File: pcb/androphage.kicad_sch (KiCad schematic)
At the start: 0 parts

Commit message: - Adapt nrfmicro schematic for control and power components. - Copy key matrix schematics from old KiCAD project.
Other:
- added sheet Control (control.kicad_sch)
- added sheet Left_Switches (left_switches.kicad_sch)
- added sheet Right_Switches (right_switches.kicad_sch)
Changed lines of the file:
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@@
 	(generator_version "9.0")
 	(paper "A4")
+	(sheet
+		(at 105.41 16.51)
+		(size 39.37 22.86)
+		(exclude_from_sim no)
+		(in_bom yes)
+		(on_board yes)
+		(dnp no)
+		(fields_autoplaced yes)
+		(stroke
+			(width 0.1524)
+			(type solid)
+		)
+		(fill
+			(color 0 0 0 0.0000)
+		)
+		(property "Sheetname" "Right_Switches"
+			(at 105.41 15.7984 0)
+			(effects
+				(font
+					(size 1.27 1.27)
+				)
+				(justify left bottom)
+			)
+		)
+		(property "Sheetfile" "right_switches.kicad_sch"
+			(at 105.41 39.9546 0)
+			(effects
+				(font
+					(size 1.27 1.27)
+				)
+				(justify left top)
+			)
+		)
+		(property "Field2" ""
+			(at 105.41 16.51 0)
+			(effects
+				(font
+					(size 1.27 1.27)
+				)
+			)
+		)
+		(instances
+			(project "androphage"
+				(path "/99196bd8-ec0c-4029-b5c4-fcab8025953e"
+					(page "4")
+				)
+			)
+		)
+	)
+	(sheet
+		(at 16.51 16.51)
+		(size 40.64 22.86)
+		(exclude_from_sim no)
+		(in_bom yes)
+		(on_board yes)
+		(dnp no)
+		(fields_autoplaced yes)
+		(stroke
+			(width 0.1524)
+			(type solid)
+		)
+		(fill
+			(color 0 0 0 0.0000)
+		)
+		(property "Sheetname" "Control"
+			(at 16.51 15.7984 0)
+			(effects
+				(font
+					(size 1.27 1.27)
+				)
+				(justify left bottom)
+			)
+		)
+		(property "Sheetfile" "control.kicad_sch"
+			(at 16.51 39.9546 0)
+			(effects
+				(font
+					(size 1.27 1.27)
+				)
+				(justify left top)
+			)
+		)
+		(instances
+			(project "androphage"
+				(path "/99196bd8-ec0c-4029-b5c4-fcab8025953e"
+					(page "2")
+				)
+			)
+		)
+	)
+	(sheet
+		(at 62.23 16.51)
+		(size 39.37 22.86)
+		(exclude_from_sim no)
+		(in_bom yes)
+		(on_board yes)
+		(dnp no)
+		(fields_autoplaced yes)
+		(stroke
+			(width 0.1524)
+			(type solid)
+		)
+		(fill
+			(color 0 0 0 0.0000)
+		)
+		(property "Sheetname" "Left_Switches"
+			(at 62.23 15.7984 0)
+			(effects
+				(font
+					(size 1.27 1.27)
+				)
+				(justify left bottom)
+			)
+		)
+		(property "Sheetfile" "left_switches.kicad_sch"
+			(at 62.23 39.9546 0)
+			(effects
+				(font
+					(size 1.27 1.27)
+				)
+				(justify left top)
+			)
+		)
+		(instances
+			(project "androphage"
+				(path "/99196bd8-ec0c-4029-b5c4-fcab8025953e"
+					(page "3")
+				)
+			)
+		)
+	)
 	(sheet_instances
 		(path "/"

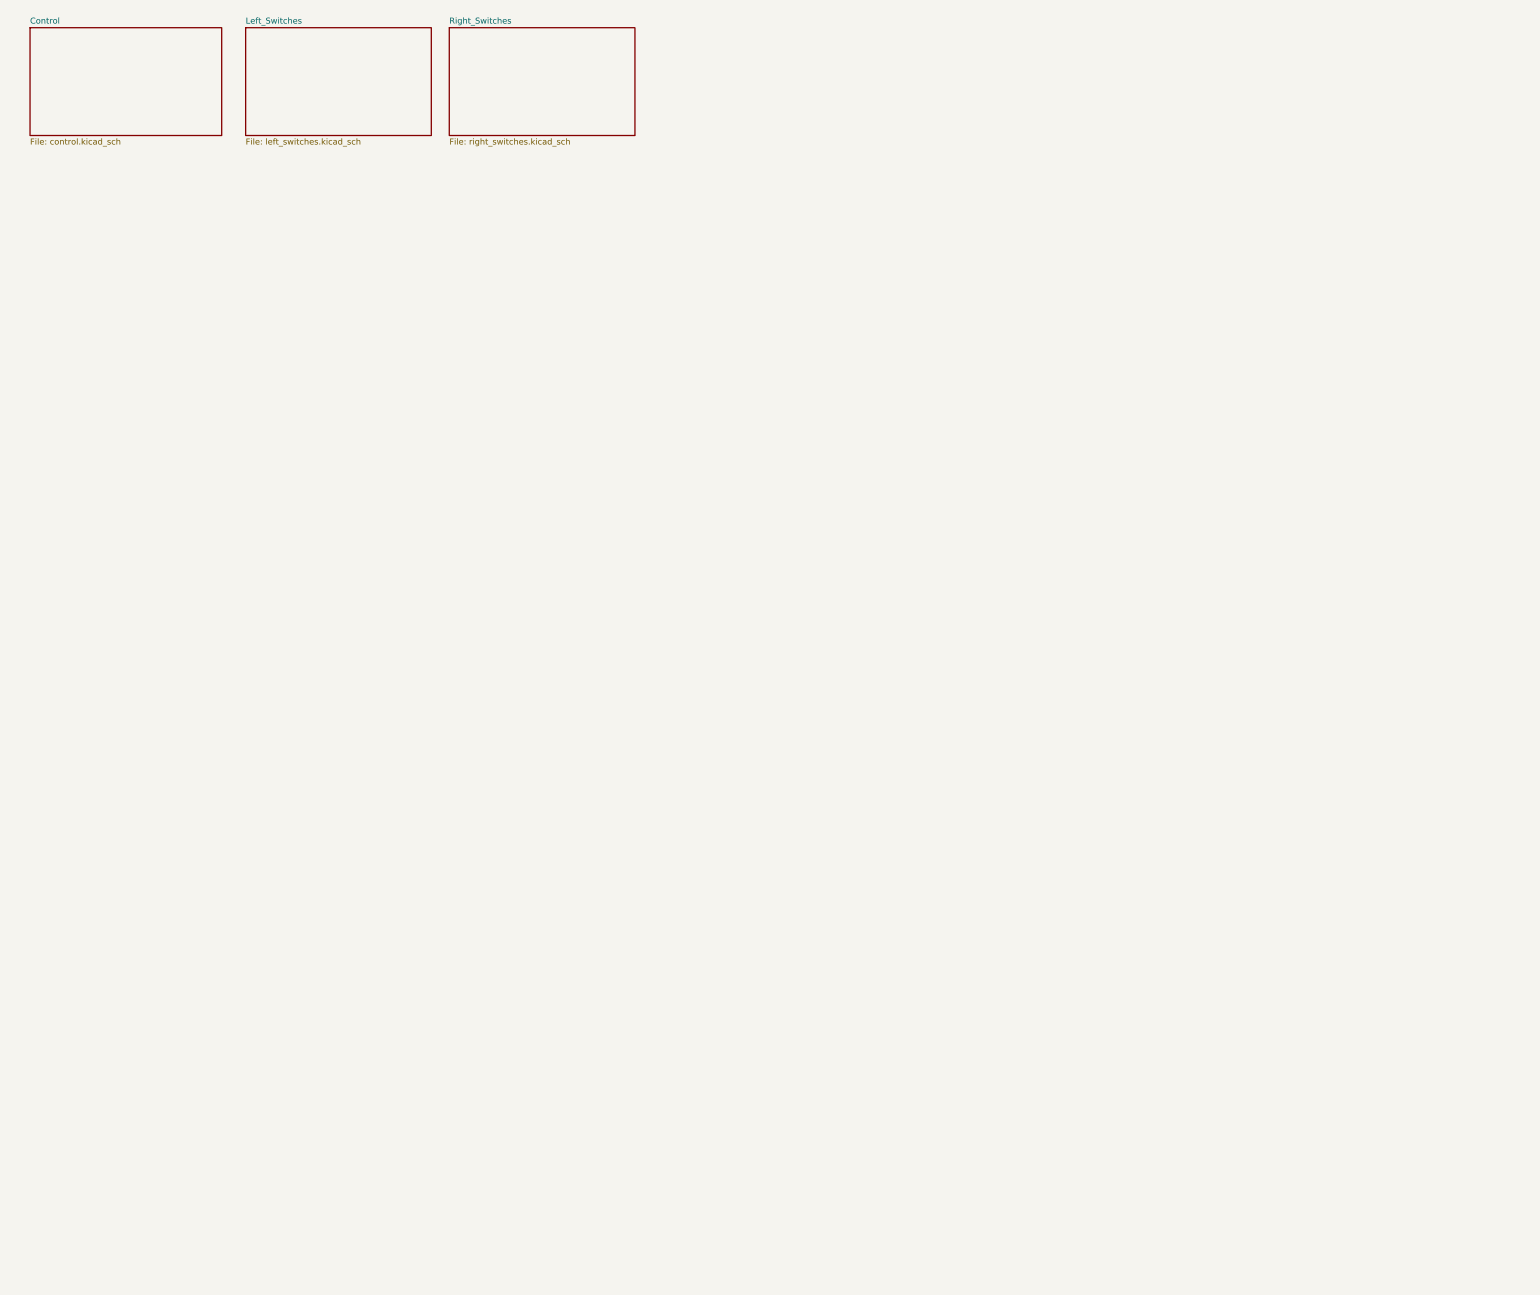
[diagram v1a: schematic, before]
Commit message: Complete preliminary PCB schematic.
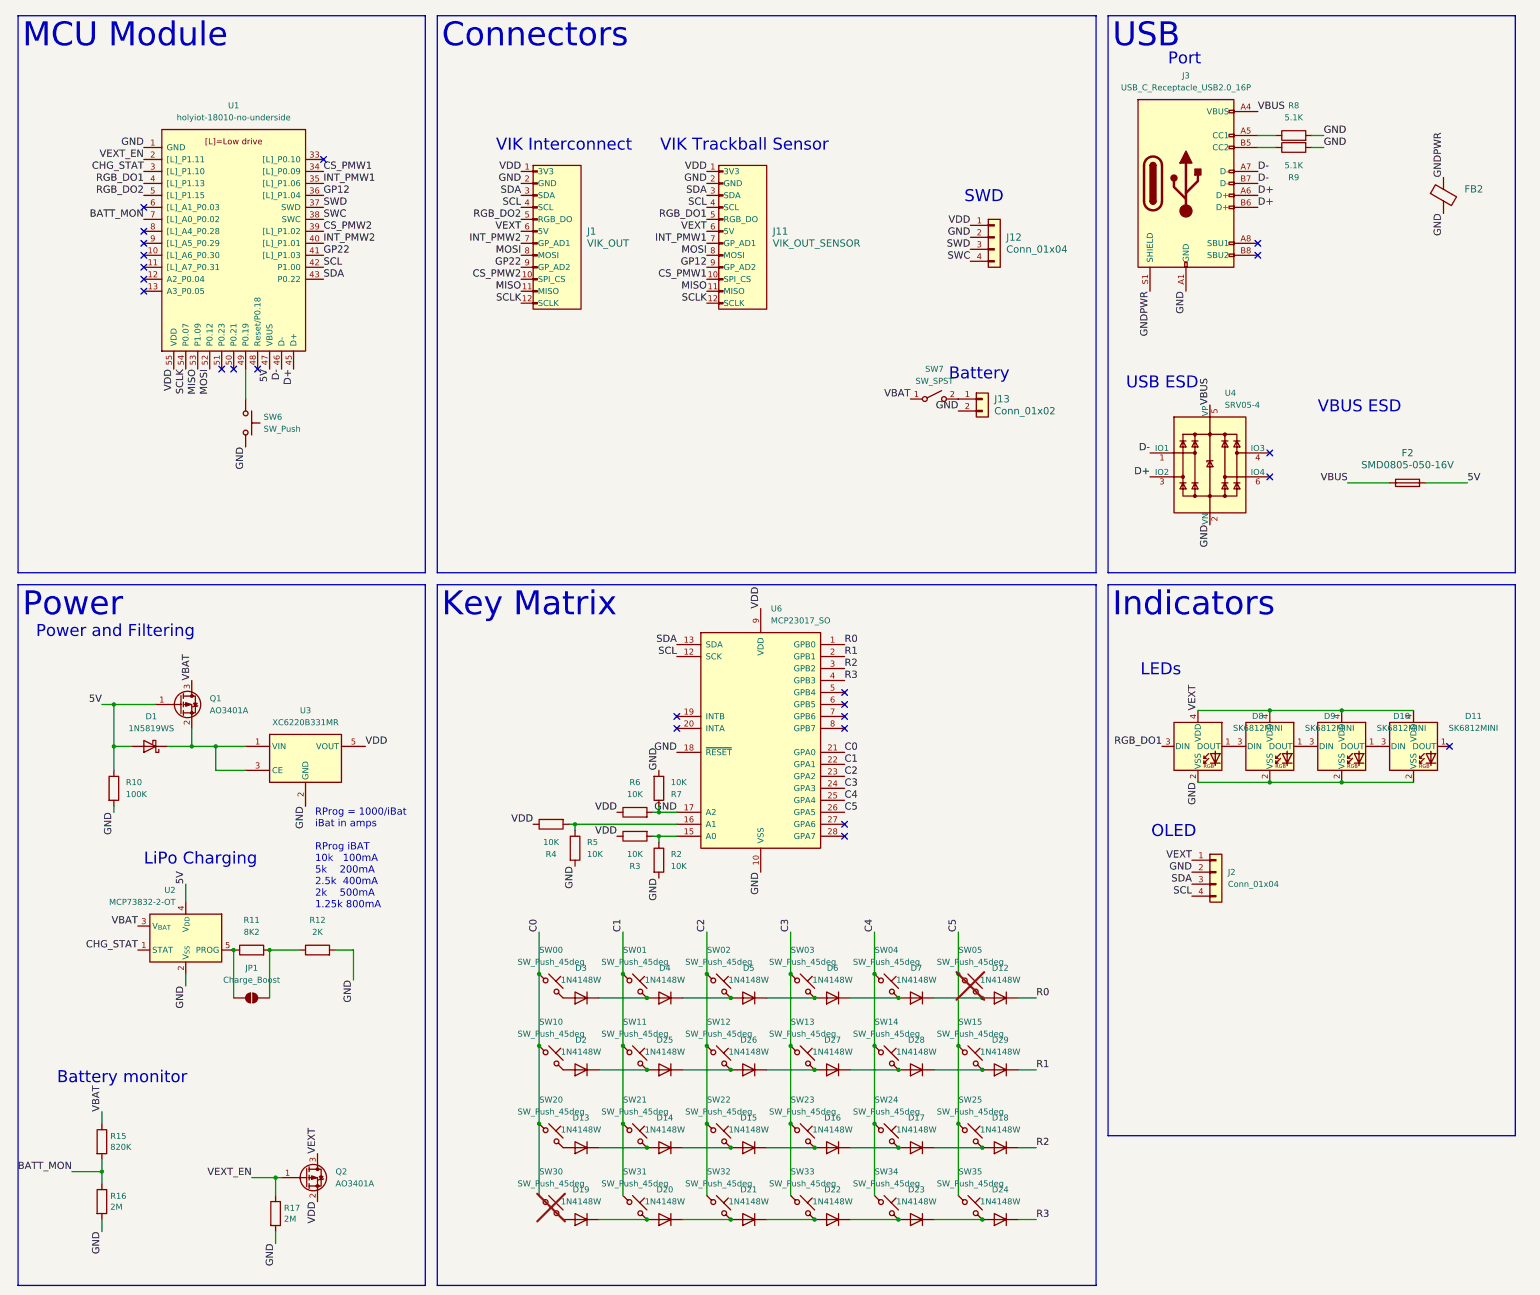
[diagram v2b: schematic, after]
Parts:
- added D1: 1N5819WS, Diode_SMD:D_SOD-323, symbol Diode:1N5819WS
- added D10, D11, D8, D9: SK6812MINI, LED_SMD:LED_SK6812MINI_PLCC4_3.5x3.5mm_P1.75mm, symbol LED:SK6812MINI
- added D12, D13, D14, D15, D16, D17, D18, D19, D2, D20, D21, D22, D23, D24, D25, D26, D27, D28, D29, D3, D4, D5, D6, D7: 1N4148W, Diode_SMD:D_SOD-123, symbol Diode:1N4148W
- added F2: SMD0805-050-16V, Fuse:Fuse_0805_2012Metric, symbol Device:Fuse
- added FB2: ~, Inductor_SMD:L_0805_2012Metric, symbol Device:FerriteBead
- added J1: VIK_OUT, vik:vik-keyboard-connector-horizontal, symbol vik:vik-keyboard-connector
- added J11: VIK_OUT_SENSOR, vik:vik-keyboard-connector-horizontal, symbol vik:vik-keyboard-connector
- added J12: Conn_01x04, Connector_PinSocket_2.54mm:PinSocket_1x04_P2.54mm_Vertical, symbol Connector_Generic:Conn_01x04
- added J13: Conn_01x02, Connector_JST:JST_GH_SM02B-GHS-TB_1x02-1MP_P1.25mm_Horizontal, symbol Connector_Generic:Conn_01x02
- added J2: Conn_01x04, Connector_JST:JST_GH_SM04B-GHS-TB_1x04-1MP_P1.25mm_Horizontal, symbol Connector_Generic:Conn_01x04
- added J3: USB_C_Receptacle_USB2.0_16P, Connector_USB:USB_C_Receptacle_HRO_TYPE-C-31-M-12, symbol Connector:USB_C_Receptacle_USB2.0_16P
- added JP1: Charge_Boost, Jumper:SolderJumper-2_P1.3mm_Open_RoundedPad1.0x1.5mm, symbol Jumper:SolderJumper_2_Open
- added Q1, Q2: AO3401A, Package_TO_SOT_SMD:SOT-23, symbol Transistor_FET:AO3401A
- added R10: 100K, Resistor_SMD:R_0201_0603Metric_Pad0.64x0.40mm_HandSolder, symbol Device:R
- added R11: 8K2, Resistor_SMD:R_0201_0603Metric_Pad0.64x0.40mm_HandSolder, symbol Device:R
- added R12: 2K, Resistor_SMD:R_0201_0603Metric_Pad0.64x0.40mm_HandSolder, symbol Device:R
- added R15: 820K, Resistor_SMD:R_0603_1608Metric, symbol Device:R
- added R16, R17: 2M, Resistor_SMD:R_0603_1608Metric, symbol Device:R
- added R2, R3, R4, R5, R6, R7: 10K, Resistor_SMD:R_0201_0603Metric_Pad0.64x0.40mm_HandSolder, symbol Device:R
- added R8, R9: 5.1K, Resistor_SMD:R_0201_0603Metric_Pad0.64x0.40mm_HandSolder, symbol Device:R
- added SW00, SW01, SW02, SW03, SW04, SW10, SW11, SW12, SW13, SW14, SW15, SW20, SW21, SW22, SW23, SW24, SW25, SW31, SW32, SW33, SW34, SW35: SW_Push_45deg, key-switches:SW_GLP_Kailh_Choc_V1V2_HotSwap_double, symbol Switch:SW_Push_45deg
- added SW05, SW30: SW_Push_45deg, symbol Switch:SW_Push_45deg
- added SW6: SW_Push, Button_Switch_SMD:SW_Push_1P1T_NO_E-Switch_TL3301NxxxxxG, symbol Switch:SW_Push
- added SW7: SW_SPST, library:AS11CH, symbol Switch:SW_SPST
- added U1: holyiot-18010-no-underside, mcu:holyiot-18010-no-underside, symbol mcu:holyiot-18010-no-underside
- added U2: MCP73832-2-OT, Package_TO_SOT_SMD:SOT-23-5, symbol Battery_Management:MCP73832-2-OT
- added U3: XC6220B331MR, Package_TO_SOT_SMD:SOT-23-5, symbol Regulator_Linear:XC6220B331MR
- added U4: SRV05-4, Package_TO_SOT_SMD:SOT-23-6, symbol Power_Protection:SRV05-4
- added U6: MCP23017_SO, Package_SO:SOIC-28W_7.5x17.9mm_P1.27mm, symbol Interface_Expansion:MCP23017_SO
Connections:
- new net: D23.1 (K), D24.2 (A), SW35.2
- new net: R4.2, R5.1, U6.16 (A1)
- new net: D6.1 (K), D7.2 (A), SW04.2
- new net: D5.1 (K), D6.2 (A), SW03.2
- new net: R2.1, R3.2, U6.15 (A0)
- new net: SW6.1, U1.49 (P0.19)
- new net: J3.A5 (CC1), R8.1
- new net: D10.1 (DOUT), D11.3 (DIN)
- new net: D10.3 (DIN), D9.1 (DOUT)
- new net: D13.2 (A), SW20.2
- new net: D16.1 (K), D17.2 (A), SW24.2
- new net: D15.1 (K), D16.2 (A), SW23.2
- new net: J3.B5 (CC2), R9.1
- new net: D27.1 (K), D28.2 (A), SW14.2
- new net: D17.1 (K), D18.2 (A), SW25.2
- new net: D22.1 (K), D23.2 (A), SW34.2
- new net: D12.2 (A), D7.1 (K), SW05.2
- new net: D4.1 (K), D5.2 (A), SW02.2
- new net: D3.1 (K), D4.2 (A), SW01.2
- new net: D28.1 (K), D29.2 (A), SW15.2
- new net: D2.1 (K), D25.2 (A), SW11.2
- new net: D2.2 (A), SW10.2
- new net: D21.1 (K), D22.2 (A), SW33.2
- new net: D19.1 (K), D20.2 (A), SW31.2
- new net: JP1.1 (A), R11.1, U2.5 (PROG)
- new net: JP1.2 (B), R11.2, R12.1
- new net: J13.1 (Pin_1), SW7.2 (B)
- new net: D25.1 (K), D26.2 (A), SW12.2
- new net: D3.2 (A), SW00.2
- new net: D13.1 (K), D14.2 (A), SW21.2
- new net: D26.1 (K), D27.2 (A), SW13.2
- new net: D19.2 (A), SW30.2
- new net: D8.1 (DOUT), D9.3 (DIN)
- new net: D14.1 (K), D15.2 (A), SW22.2
- new net: D20.1 (K), D21.2 (A), SW32.2
- new net: D1.1 (K), Q1.2 (S), U3.1 (VIN), U3.3 (CE)
- new net 5V: D1.2 (A), F2.2, Q1.1 (G), R10.1, U1.47 (VBUS), U2.4 (V_{DD})
- new net BATT_MON: R15.2, R16.1, U1.7 ([L]_A0_P0.02)
- new net C0: SW00.1, SW10.1, SW20.1, SW30.1, U6.21 (GPA0)
- new net C1: SW01.1, SW11.1, SW21.1, SW31.1, U6.22 (GPA1)
- new net C2: SW02.1, SW12.1, SW22.1, SW32.1, U6.23 (GPA2)
- new net C3: SW03.1, SW13.1, SW23.1, SW33.1, U6.24 (GPA3)
- new net C4: SW04.1, SW14.1, SW24.1, SW34.1, U6.25 (GPA4)
- new net C5: SW05.1, SW15.1, SW25.1, SW35.1, U6.26 (GPA5)
- new net CHG_STAT: U1.3 ([L]_P1.10), U2.1 (STAT)
- new net CS_PMW1: J11.10 (SPI_CS), U1.34 ([L]_P0.09)
- new net CS_PMW2: J1.10 (SPI_CS), U1.39 ([L]_P1.02)
- new net D+: J3.A6 (D+), J3.B6 (D+), U1.45 (D+), U4.3 (IO2)
- new net D-: J3.A7 (D-), J3.B7 (D-), U1.46 (D-), U4.1 (IO1)
- new net GND: D10.2 (VSS), D11.2 (VSS), D8.2 (VSS), D9.2 (VSS), FB2.2, J1.2 (GND), J11.2 (GND), J12.2 (Pin_2), J13.2 (Pin_2), J2.2 (Pin_2), J3.A1 (GND), J3.A12 (GND), J3.B1 (GND), J3.B12 (GND), R10.2, R12.2, R16.2, R17.2, R2.2, R5.2, R6.2, R7.1, R7.2, R8.2, R9.2, SW6.2, U1.1 (GND), U1.32 (GND), U1.44 (GND), U2.2 (V_{SS}), U3.2 (GND), U4.2 (VN), U6.10 (VSS), U6.17 (A2), U6.18 (~{RESET})
- new net GNDPWR: FB2.1, J3.S1 (SHIELD)
- new net GP12: J11.9 (GP_AD2), U1.36 ([L]_P1.04)
- new net GP22: J1.9 (GP_AD2), U1.41 ([L]_P1.03)
- new net INT_PMW1: J11.7 (GP_AD1), U1.35 ([L]_P1.06)
- new net INT_PMW2: J1.7 (GP_AD1), U1.40 ([L]_P1.01)
- new net MISO: J1.11 (MISO), J11.11 (MISO), U1.53 (P1.09)
- new net MOSI: J1.8 (MOSI), J11.8 (MOSI), U1.52 (P0.12)
- new net R0: D12.1 (K), U6.1 (GPB0)
- new net R1: D29.1 (K), U6.2 (GPB1)
- new net R2: D18.1 (K), U6.3 (GPB2)
- new net R3: D24.1 (K), U6.4 (GPB3)
- new net RGB_DO1: D8.3 (DIN), J11.5 (RGB_DO), U1.4 ([L]_P1.13)
- new net RGB_DO2: J1.5 (RGB_DO), U1.5 ([L]_P1.15)
- new net SCL: J1.4 (SCL), J11.4 (SCL), J2.4 (Pin_4), U1.42 (P1.00), U6.12 (SCK)
- new net SCLK: J1.12 (SCLK), J11.12 (SCLK), U1.54 (P0.07)
- new net SDA: J1.3 (SDA), J11.3 (SDA), J2.3 (Pin_3), U1.43 (P0.22), U6.13 (SDA)
- new net SWC: J12.4 (Pin_4), U1.38 (SWC)
- new net SWD: J12.3 (Pin_3), U1.37 (SWD)
- new net VBAT: Q1.3 (D), R15.1, SW7.1 (A), U2.3 (V_{BAT})
- new net VBUS: F2.1, J3.A4 (VBUS), J3.A9 (VBUS), J3.B4 (VBUS), J3.B9 (VBUS), U4.5 (VP)
- new net VDD: J1.1 (3V3), J11.1 (3V3), J12.1 (Pin_1), Q2.2 (S), R3.1, R4.1, R6.1, U1.55 (VDD), U3.5 (VOUT), U6.9 (VDD)
- new net VEXT: D10.4 (VDD), D11.4 (VDD), D8.4 (VDD), D9.4 (VDD), J1.6 (5V), J11.6 (5V), J2.1 (Pin_1), Q2.3 (D)
- new net VEXT_EN: Q2.1 (G), R17.1, U1.2 ([L]_P1.11)
- no-connect marks 0 -> 24
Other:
- removed sheet Control
- removed sheet Left_Switches
- removed sheet Right_Switches
- note added: "Battery"
- note added: "Battery monitor"
- note added: "LEDs"
- note added: "LiPo Charging"
- note added: "OLED"
- note added: "Port"
- note added: "Power and Filtering"
- note added: "RProg = 1000/iBat iBat in amps RProg iBAT 10k 100mA 5k 200mA 2.5k 400mA 2k 500mA 1.25k 800mA"
- note added: "SWD"
- note added: "USB ESD"
- note added: "VBUS ESD"
- note added: "VIK Interconnect"
- note added: "VIK Trackball Sensor"

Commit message: Start PCB layout.
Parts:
- added R1: 10K, Resistor_SMD:R_0201_0603Metric_Pad0.64x0.40mm_HandSolder, symbol Device:R
- U6: value MCP23017_SO -> MCP23017_SS; footprint Package_SO:SOIC-28W_7.5x17.9mm_P1.27mm -> Package_SO:SSOP-28_5.3x10.2mm_P0.65mm; symbol Interface_Expansion:MCP23017_SO -> Interface_Expansion:MCP23017_SS
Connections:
- net GND: no longer U6.18 (~{RESET})
- net VDD: now also R1.1
- new net: R1.2, U6.18 (~{RESET})
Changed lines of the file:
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@@
 	(wire
 		(pts
+			(xy 151.13 167.64) (xy 151.13 170.18)
+		)
+		(stroke
+			(width 0)
+			(type default)
+		)
+	)
+	(wire
+		(pts
 			(xy 172.72 254) (xy 182.88 254)
 		)
@@
 	(wire
 		(pts
+			(xy 151.13 170.18) (xy 153.67 170.18)
+		)
+		(stroke
+			(width 0)
+			(type default)
+		)
+	)
+	(wire
+		(pts
 			(xy 132.08 186.69) (xy 132.08 185.42)
 		)
@@
 		)
 	)
-	(label "GND"
-		(at 153.67 170.18 180)
-		(effects
-			(font
-				(size 1.524 1.524)
-			)
-			(justify right bottom)
-		)
-	)
 	(label "VDD"
 		(at 140.97 182.88 180)
@@
 		)
 	)
+	(label "VDD"
+		(at 143.51 167.64 180)
+		(effects
+			(font
+				(size 1.524 1.524)
+			)
+			(justify right bottom)
+		)
+	)
 	(symbol
 		(lib_id "Switch:SW_Push_45deg")
@@
 	)
 	(symbol
-		(lib_id "Interface_Expansion:MCP23017_SO")
+		(lib_id "Interface_Expansion:MCP23017_SS")
 		(at 171.45 167.64 0)
 		(unit 1)
@@
 			)
 		)
-		(property "Value" "MCP23017_SO"
+		(property "Value" "MCP23017_SS"
 			(at 173.5933 142.24 0)
 			(effects
@@
 			)
 		)
-		(property "Footprint" "Package_SO:SOIC-28W_7.5x17.9mm_P1.27mm"
+		(property "Footprint" "Package_SO:SSOP-28_5.3x10.2mm_P0.65mm"
 			(at 176.53 193.04 0)
 			(effects
@@
 			)
 		)
-		(property "Description" "16-bit I/O expander, I2C, interrupts, w pull-ups, GPA/B7 output only (https://microchip.my.site.com/s/article/GPA7---GPB7-Cannot-Be-Used-as-Inputs-In-MCP23017),  SOIC-28"
+		(property "Description" "16-bit I/O expander, I2C, interrupts, w pull-ups, SSOP-28"
 			(at 171.45 167.64 0)
 			(effects
@@
 					(unit 1)
 				)
+			)
+		)
+	)
+	(symbol
+		(lib_id "Device:R")
+		(at 147.32 167.64 90)
+		(unit 1)
+		(exclude_from_sim no)
+		(in_bom yes)
+		(on_board yes)
+		(dnp no)
+		(property "Reference" "R1"
+			(at 147.32 161.29 90)
+			(effects
+				(font
+					(size 1.27 1.27)
+				)
+			)
+		)
+		(property "Value" "10K"
+			(at 147.32 163.83 90)
+			(effects
+				(font
+					(size 1.27 1.27)
+				)
+			)
+		)
+		(property "Footprint" "Resistor_SMD:R_0201_0603Metric_Pad0.64x0.40mm_HandSolder"
+			(at 147.32 169.418 90)
+			(effects
+				(font
+					(size 1.27 1.27)
+				)
+				(hide yes)
+			)
+		)
+		(property "Datasheet" "~"
+			(at 147.32 167.64 0)
+			(effects
+				(font
+					(size 1.27 1.27)
+				)
+				(hide yes)
+			)
+		)
+		(property "Description" "Resistor"
+			(at 147.32 167.64 0)
+			(effects
+				(font
+					(size 1.27 1.27)
+				)
+				(hide yes)
+			)
+		)
+		(pin "2"
+		)
+		(pin "1"
+		)
+		(instances
+			(project "androphage"
+				(path "/99196bd8-ec0c-4029-b5c4-fcab8025953e"
+					(reference "R1")
+					(unit 1)
+				)
